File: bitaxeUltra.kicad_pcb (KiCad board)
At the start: 4 copper layers, 56.5 x 99.8 mm, 140 parts, among them J1 54-00164, J2 TC2030-IDC, J3 Conn_01x04, J4 Conn_01x06, J5 USB_C_Receptacle_USB2.0, J6 Conn_01x04, Q1 MMBT3904, SW1 GT-TC029B-H025-L1N, SW2 GT-TC029B-H025-L1N, T1 net-tie, U10 EMC2101, U12 BM1366_mode1, U2 TPS546D24ARVFR, U3 RT9080-33GJ5, U4 ESP32-S3-WROOM-1, U5 MCP1824T-1202E/OT, U6 MCP1824T-0802E, U7 25MHz, U9 SN74AVC4T774

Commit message: Add TCH logo
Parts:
- added REF**: TCH-Logo-Mask, bitaxe:TCH-Logo-Mask, B.Cu at (114.5, 143.4)
- added REF**: TCH-Logo, bitaxe:TCH-Logo, B.Cu at (114.5, 142.8)

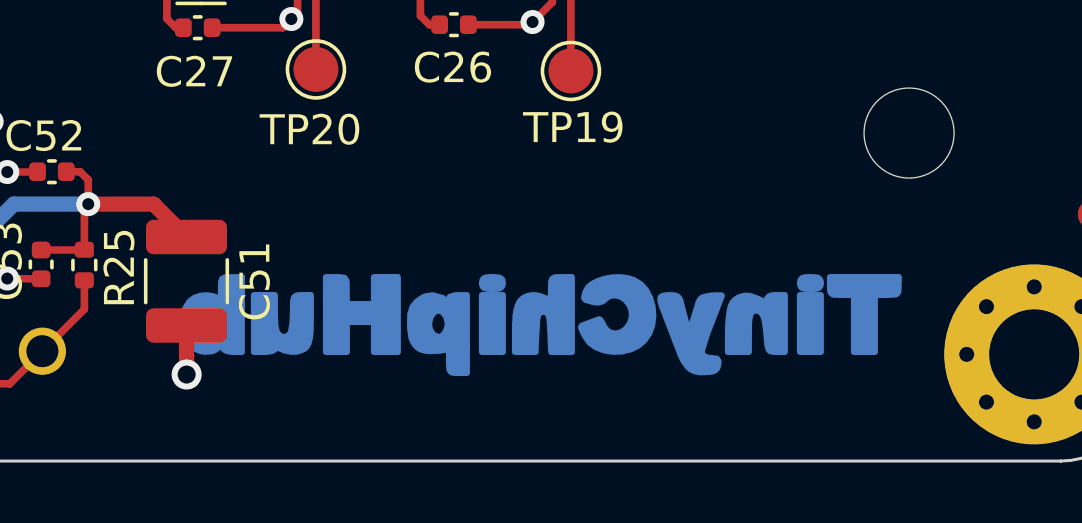
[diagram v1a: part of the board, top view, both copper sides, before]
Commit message: Change logo for to B
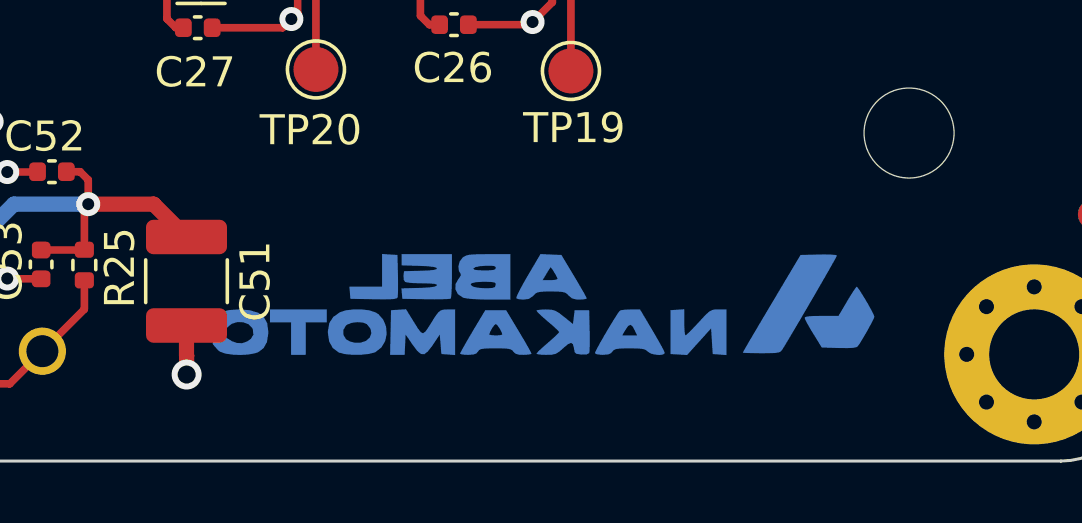
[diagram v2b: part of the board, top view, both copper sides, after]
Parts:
- removed REF**: TCH-Logo-Mask, bitaxe:TCH-Logo-Mask
- removed REF**: TCH-Logo, bitaxe:TCH-Logo
- added G*** (x2): LOGO, LOGO, B.Cu at (113.8, 142.1)

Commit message: finalize
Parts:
- removed the G*** at (105.1, 89.7) (x2)
- added G*** (x2): LOGO, LOGO, B.Cu at (105.0, 90.9)
- moved G*** 2.39 mm to (114.0, 144.5) (x2)
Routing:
- net GND: track 91.4 -> 89.5 mm
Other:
- board text removed: "207"
